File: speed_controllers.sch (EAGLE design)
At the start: 9 parts

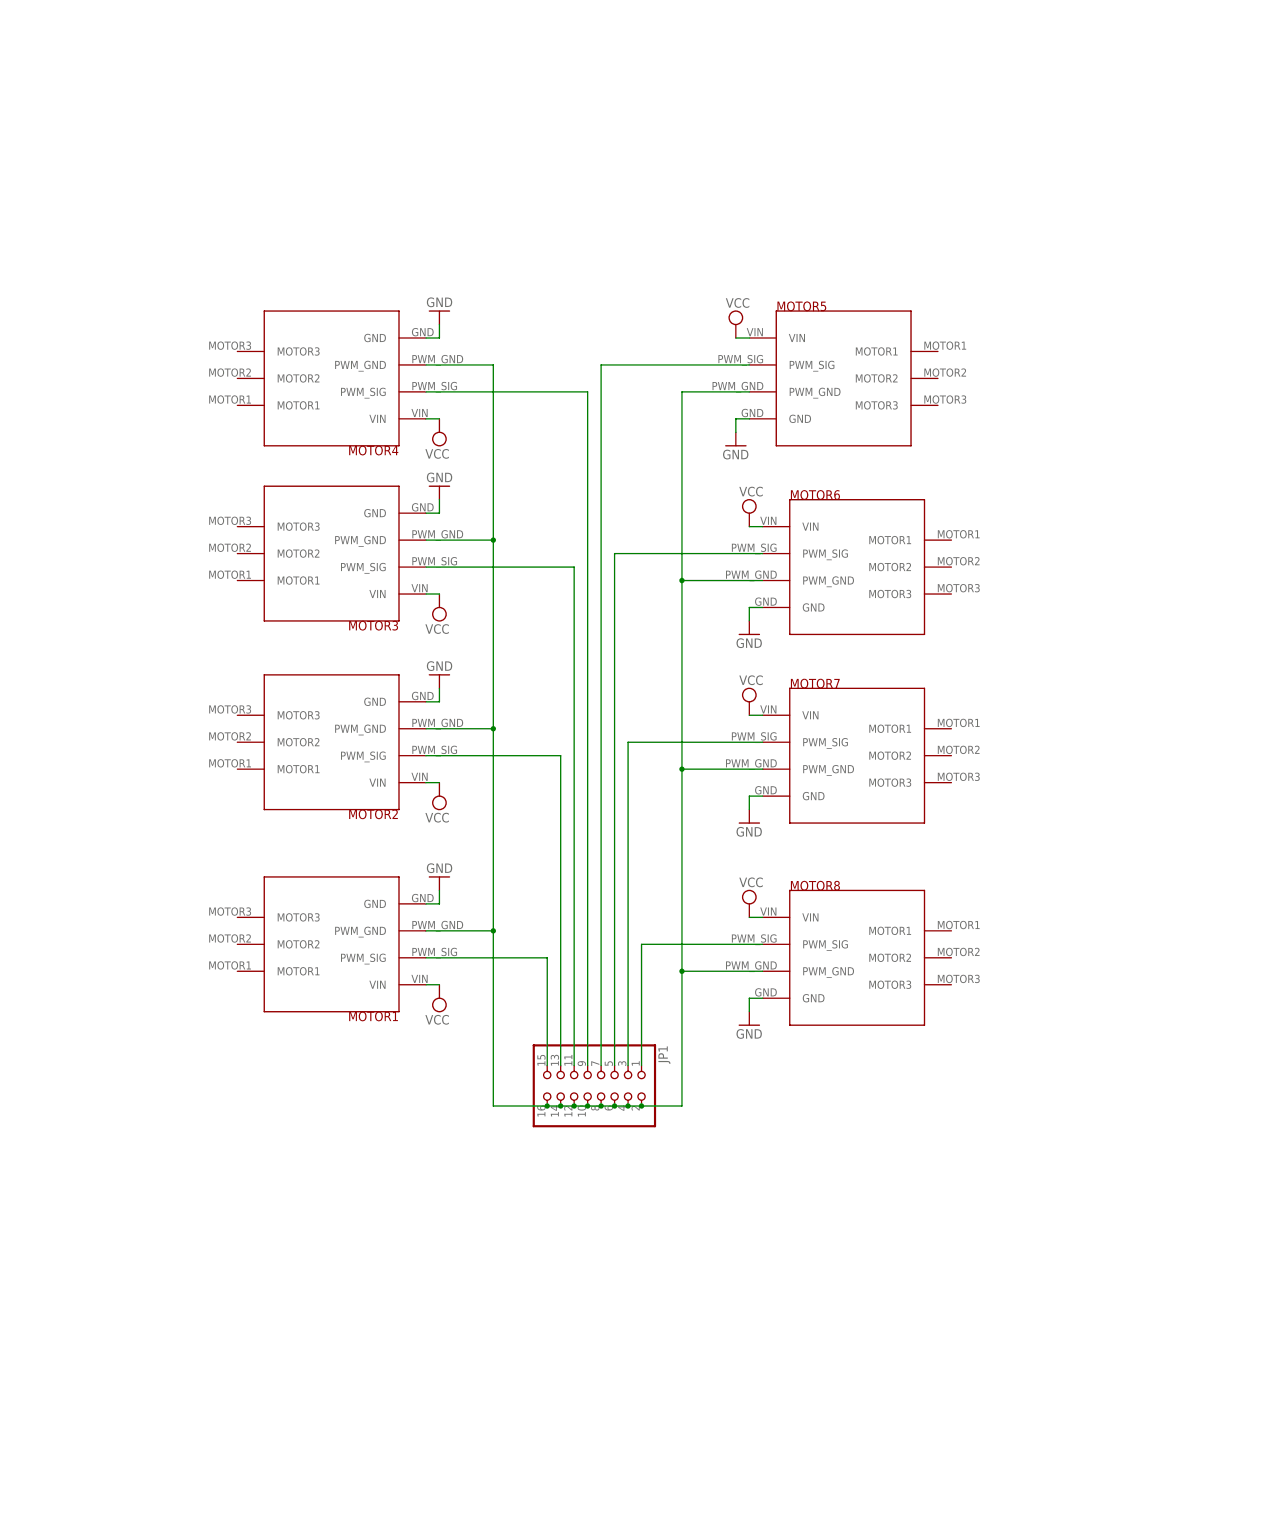
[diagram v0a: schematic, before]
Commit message: Redid ESC boards
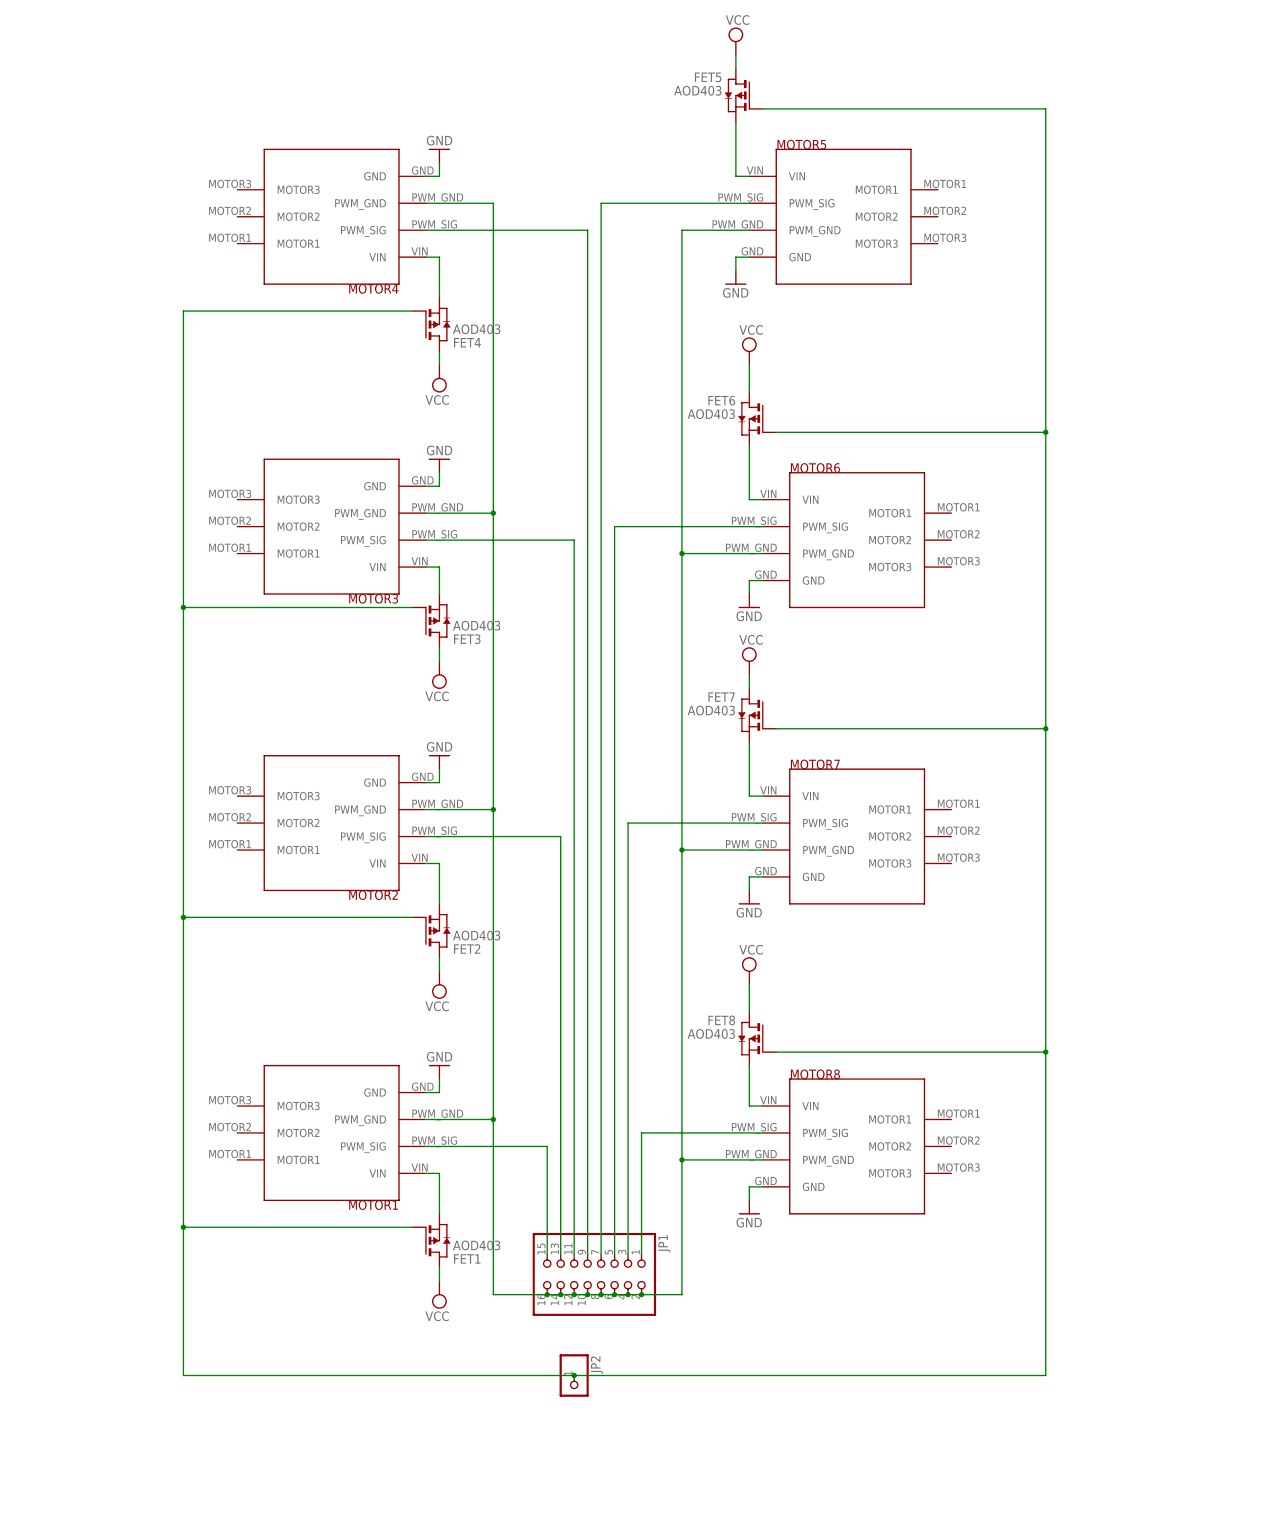
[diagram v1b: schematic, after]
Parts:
- added FET1, FET2, FET3, FET4, FET5, FET6, FET7, FET8: AOD403, auv:AOD403
- added JP2: (no value), auv:PINHD-1X1
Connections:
- new net N$10: FET1.S, MOTOR1.VIN
- new net N$12: FET2.S, MOTOR2.VIN
- new net N$13: FET3.S, MOTOR3.VIN
- new net N$14: FET4.S, MOTOR4.VIN
- new net N$15: FET5.S, MOTOR5.VIN
- new net N$16: FET6.S, MOTOR6.VIN
- new net N$17: FET7.S, MOTOR7.VIN
- new net N$18: FET8.S, MOTOR8.VIN
- new net N$20: FET1.G, FET2.G, FET3.G, FET4.G, FET5.G, FET6.G, FET7.G, FET8.G, JP2.1
- net VCC: now also FET1.D, FET2.D, FET3.D, FET4.D, FET5.D, FET6.D, FET7.D, FET8.D; no longer MOTOR1.VIN, MOTOR2.VIN, MOTOR3.VIN, MOTOR4.VIN, MOTOR5.VIN, MOTOR6.VIN, MOTOR7.VIN, MOTOR8.VIN
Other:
- moved on the sheet: JP1, MOTOR1, MOTOR2, MOTOR3, MOTOR4, MOTOR5, MOTOR6, MOTOR7, MOTOR8

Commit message: ESC Board
Features:
* 8 ESC's
* XT60 battery connector P-Channel mosfets for kill switch
* Hall effect kill switch
* LED Kill switch indicators
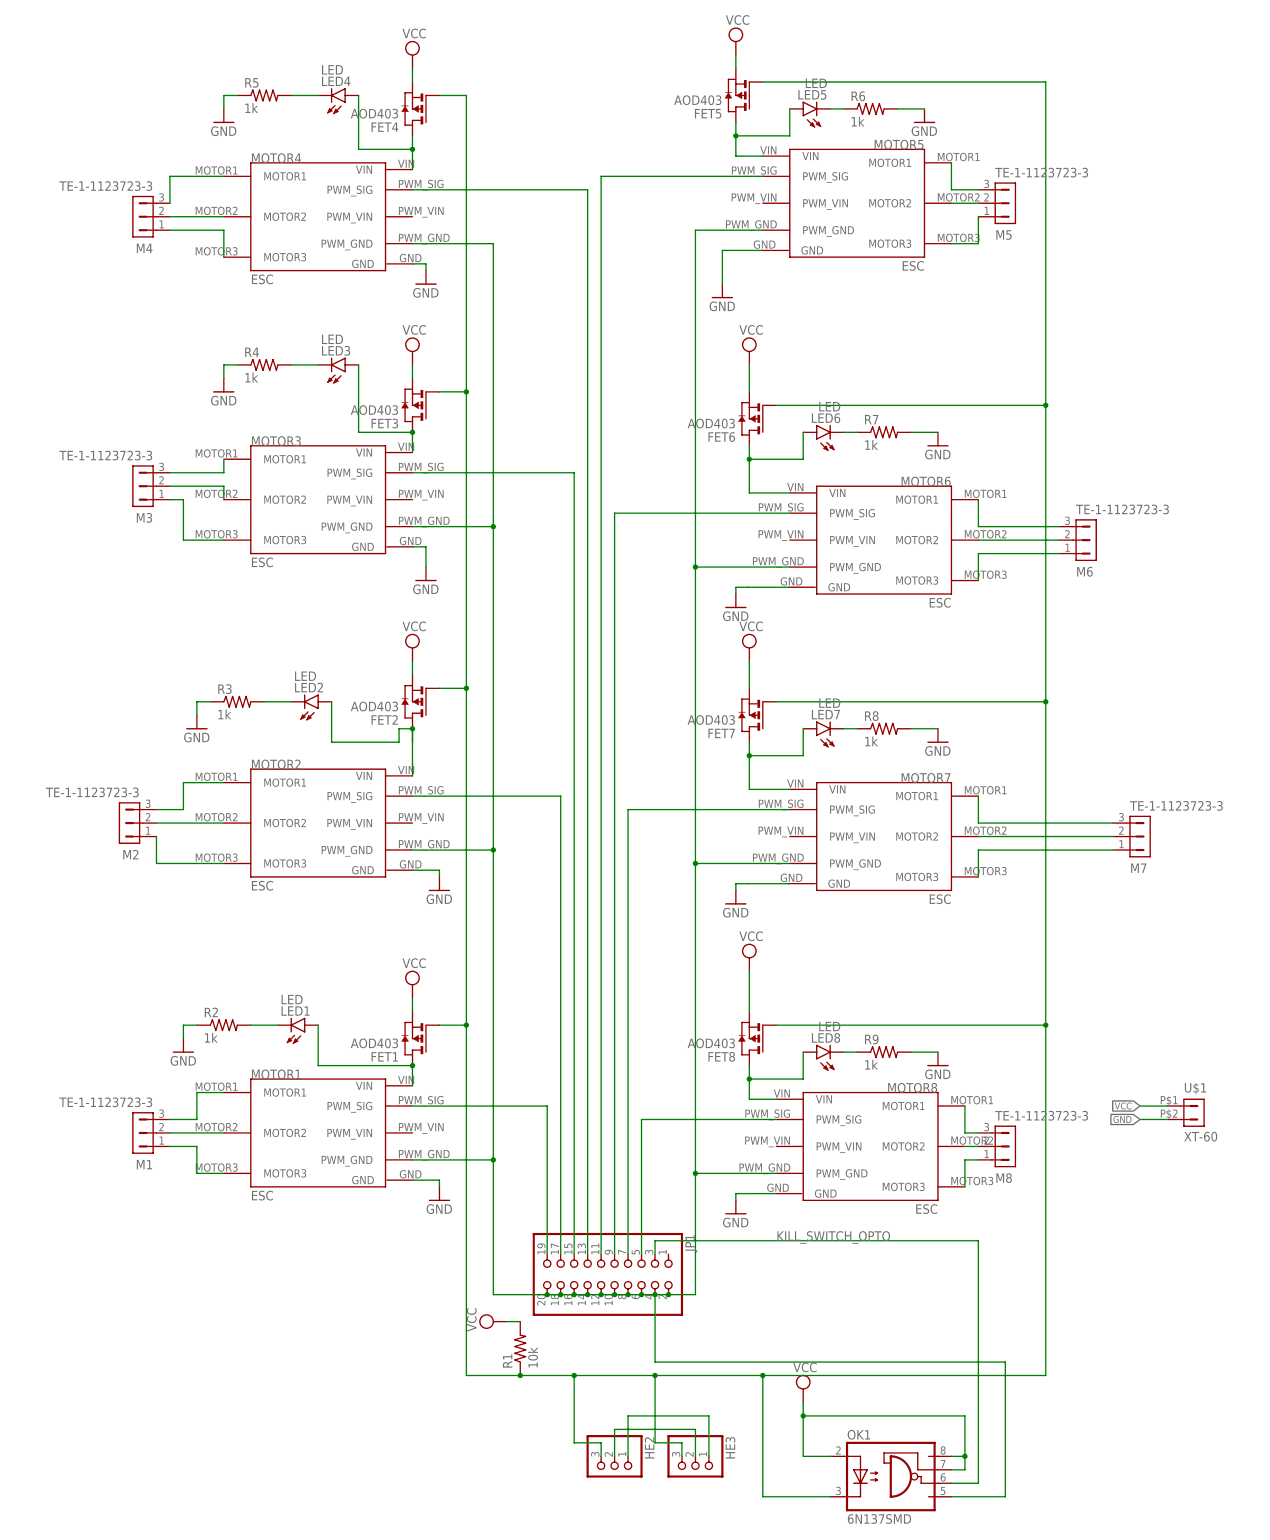
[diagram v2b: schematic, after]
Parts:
- removed JP2: (no value), auv:PINHD-1X1
- added HE2, HE3: (no value), auv:PINHD-1X3
- added LED1, LED2, LED3, LED4, LED5, LED6, LED7, LED8: LED, auv:LED
- added M1, M2, M3, M4, M5, M6, M7, M8: TE-1-1123723-3, auv:TE-1-1123723-3
- added OK1: 6N137SMD, auv:6N137SMD
- added R1: 10k, auv:R-US_R0603
- added R2, R3, R4, R5, R6, R7, R8, R9: 1k, auv:R-US_R0603
- added U$1: XT-60, auv:XT-60
- JP1: device auv:PINHD-2X8 -> auv:PINHD-2X10
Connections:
- removed net N$1: JP1.15, MOTOR1.PWM_SIG
- removed net N$10: FET1.S, MOTOR1.VIN
- removed net N$14: FET4.S, MOTOR4.VIN
- removed net N$15: FET5.S, MOTOR5.VIN
- removed net N$16: FET6.S, MOTOR6.VIN
- removed net N$17: FET7.S, MOTOR7.VIN
- removed net N$18: FET8.S, MOTOR8.VIN
- removed net N$2: JP1.13, MOTOR2.PWM_SIG
- removed net N$20: FET1.G, FET2.G, FET3.G, FET4.G, FET5.G, FET6.G, FET7.G, FET8.G, JP2.1
- removed net N$3: JP1.11, MOTOR3.PWM_SIG
- removed net N$4: JP1.9, MOTOR4.PWM_SIG
- removed net N$5: JP1.7, MOTOR5.PWM_SIG
- new net FET_G: FET1.G, FET2.G, FET3.G, FET4.G, FET5.G, FET6.G, FET7.G, FET8.G, HE2.3, HE3.3, OK1.C, R1.1
- new net KILL_SWITCH_OPTO: JP1.3, OK1.VO
- new net M1_1: M1.1, MOTOR1.MOTOR3
- new net M1_2: M1.2, MOTOR1.MOTOR2
- new net M1_3: M1.3, MOTOR1.MOTOR1
- new net M2_1: M2.1, MOTOR2.MOTOR3
- new net M2_2: M2.2, MOTOR2.MOTOR2
- new net M2_3: M2.3, MOTOR2.MOTOR1
- new net M3_1: M3.1, MOTOR3.MOTOR3
- new net M3_2: M3.2, MOTOR3.MOTOR2
- new net M3_3: M3.3, MOTOR3.MOTOR1
- new net M4_1: M4.1, MOTOR4.MOTOR3
- new net M4_2: M4.2, MOTOR4.MOTOR2
- new net M4_3: M4.3, MOTOR4.MOTOR1
- new net M5_1: M5.1, MOTOR5.MOTOR3
- new net M5_2: M5.2, MOTOR5.MOTOR2
- new net M5_3: M5.3, MOTOR5.MOTOR1
- new net M6_1: M6.1, MOTOR6.MOTOR3
- new net M6_2: M6.2, MOTOR6.MOTOR2
- new net M6_3: M6.3, MOTOR6.MOTOR1
- new net M7_1: M7.1, MOTOR7.MOTOR3
- new net M7_2: M7.2, MOTOR7.MOTOR2
- new net M7_3: M7.3, MOTOR7.MOTOR1
- new net M8_1: M8.1, MOTOR8.MOTOR3
- new net M8_2: M8.2, MOTOR8.MOTOR2
- new net M8_3: M8.3, MOTOR8.MOTOR1
- new net N$11: LED5.C, R6.1
- new net PWM_GND: JP1.10, JP1.12, JP1.14, JP1.16, JP1.18, JP1.2, JP1.20, JP1.4, JP1.6, JP1.8, MOTOR1.PWM_GND, MOTOR2.PWM_GND, MOTOR3.PWM_GND, MOTOR4.PWM_GND, MOTOR5.PWM_GND, MOTOR6.PWM_GND, MOTOR7.PWM_GND, MOTOR8.PWM_GND, OK1.GND
- new net R7: LED6.C, R7.1
- new net SIG_1: JP1.19, MOTOR1.PWM_SIG
- new net SIG_2: JP1.17, MOTOR2.PWM_SIG
- new net SIG_3: JP1.15, MOTOR3.PWM_SIG
- new net SIG_4: JP1.13, MOTOR4.PWM_SIG
- new net SIG_5: JP1.11, MOTOR5.PWM_SIG
- new net SIG_6: JP1.9, MOTOR6.PWM_SIG
- new net SIG_7: JP1.7, MOTOR7.PWM_SIG
- new net SIG_8: JP1.5, MOTOR8.PWM_SIG
- new net VIN3: FET3.D, LED3.A, MOTOR3.VIN
- new net VIN_1: FET1.D, LED1.A, MOTOR1.VIN
- new net VIN_2: FET2.D, LED2.A, MOTOR2.VIN
- new net VIN_4: FET4.D, LED4.A, MOTOR4.VIN
- new net VIN_5: FET5.D, LED5.A, MOTOR5.VIN
- new net VIN_6: FET6.D, LED6.A, MOTOR6.VIN
- new net VIN_7: FET7.D, LED7.A, MOTOR7.VIN
- new net VIN_8: FET8.D, LED8.A, MOTOR8.VIN
- net GND: now also HE2.2, HE3.2, R2.1, R3.1, R4.1, R5.1, R6.2, R7.2, R8.2, R9.2, U$1.2
- net N$12: now also LED7.C, R8.1; no longer FET2.S, MOTOR2.VIN
- net N$13: now also LED8.C, R9.1; no longer FET3.S, MOTOR3.VIN
- net N$6: now also LED1.C, R2.2; no longer JP1.5, MOTOR6.PWM_SIG
- net N$7: now also LED2.C, R3.2; no longer JP1.3, MOTOR7.PWM_SIG
- net N$8: now also LED3.C, R4.2; no longer JP1.1, MOTOR8.PWM_SIG
- net N$9: now also LED4.C, R5.2; no longer JP1.10, JP1.12, JP1.14, JP1.16, JP1.2, JP1.4, JP1.6, JP1.8, MOTOR1.PWM_GND, MOTOR2.PWM_GND, MOTOR3.PWM_GND, MOTOR4.PWM_GND, MOTOR5.PWM_GND, MOTOR6.PWM_GND, MOTOR7.PWM_GND, MOTOR8.PWM_GND
- net VCC: now also FET1.S, FET2.S, HE2.1, HE3.1, OK1.A, OK1.VCC, OK1.VE, R1.2, U$1.1; no longer FET1.D, FET2.D, FET3.D, FET4.D, FET5.D, FET6.D, FET7.D, FET8.D
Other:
- moved on the sheet: FET1, FET2, FET3, FET4, FET5, FET6, FET7, FET8

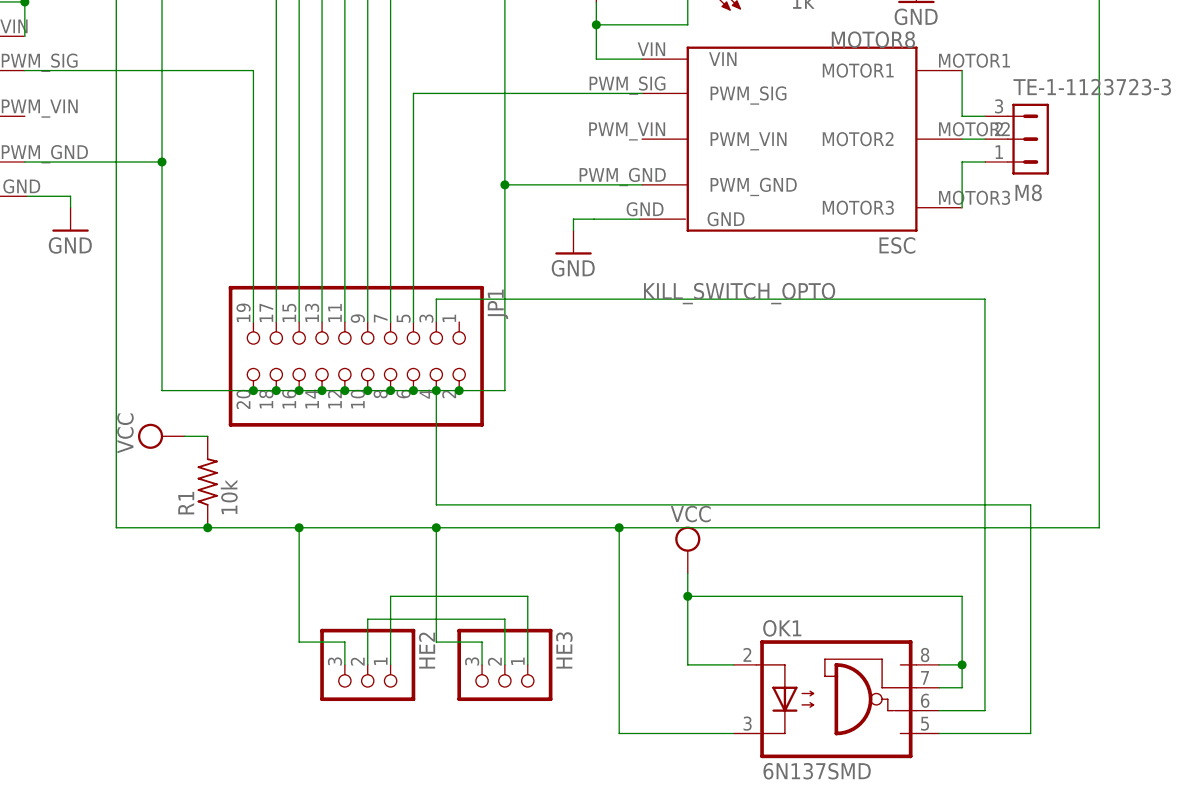
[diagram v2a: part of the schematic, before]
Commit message: Changed Optocoupler circuit
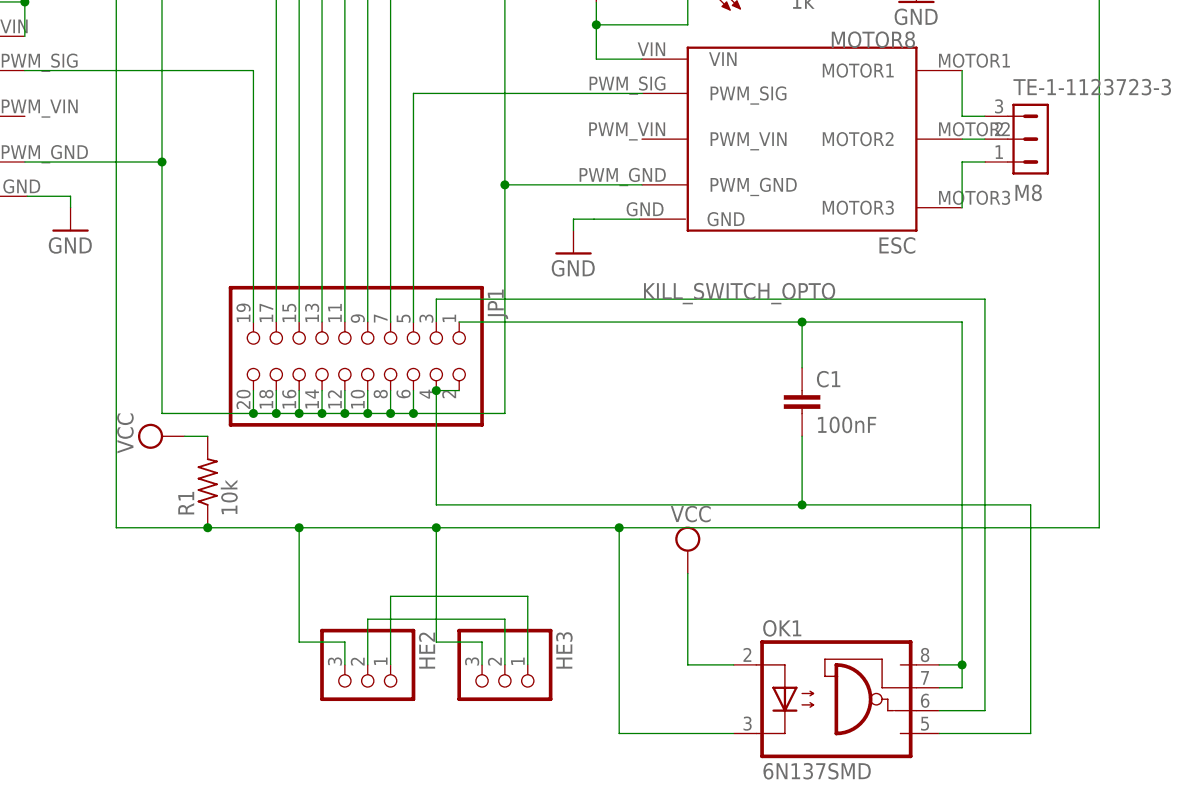
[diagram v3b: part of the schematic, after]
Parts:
- added C1: 100nF, rcl:C-EUC0603
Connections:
- new net MCU_GND: C1.2, JP1.2, JP1.4, OK1.GND
- new net MCU_VCC: C1.1, JP1.1, OK1.VCC, OK1.VE
- net PWM_GND: no longer JP1.2, JP1.4, OK1.GND
- net VCC: no longer OK1.VCC, OK1.VE
